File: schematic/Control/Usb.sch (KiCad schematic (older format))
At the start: 35 parts

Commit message: Control board diagram complete at high level - Clock, USB, Control, Power and IO done. Remaining is FPGA pin assignment which will be done later to optimize board layout.
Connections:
- net +3V3_USB renamed +3V3

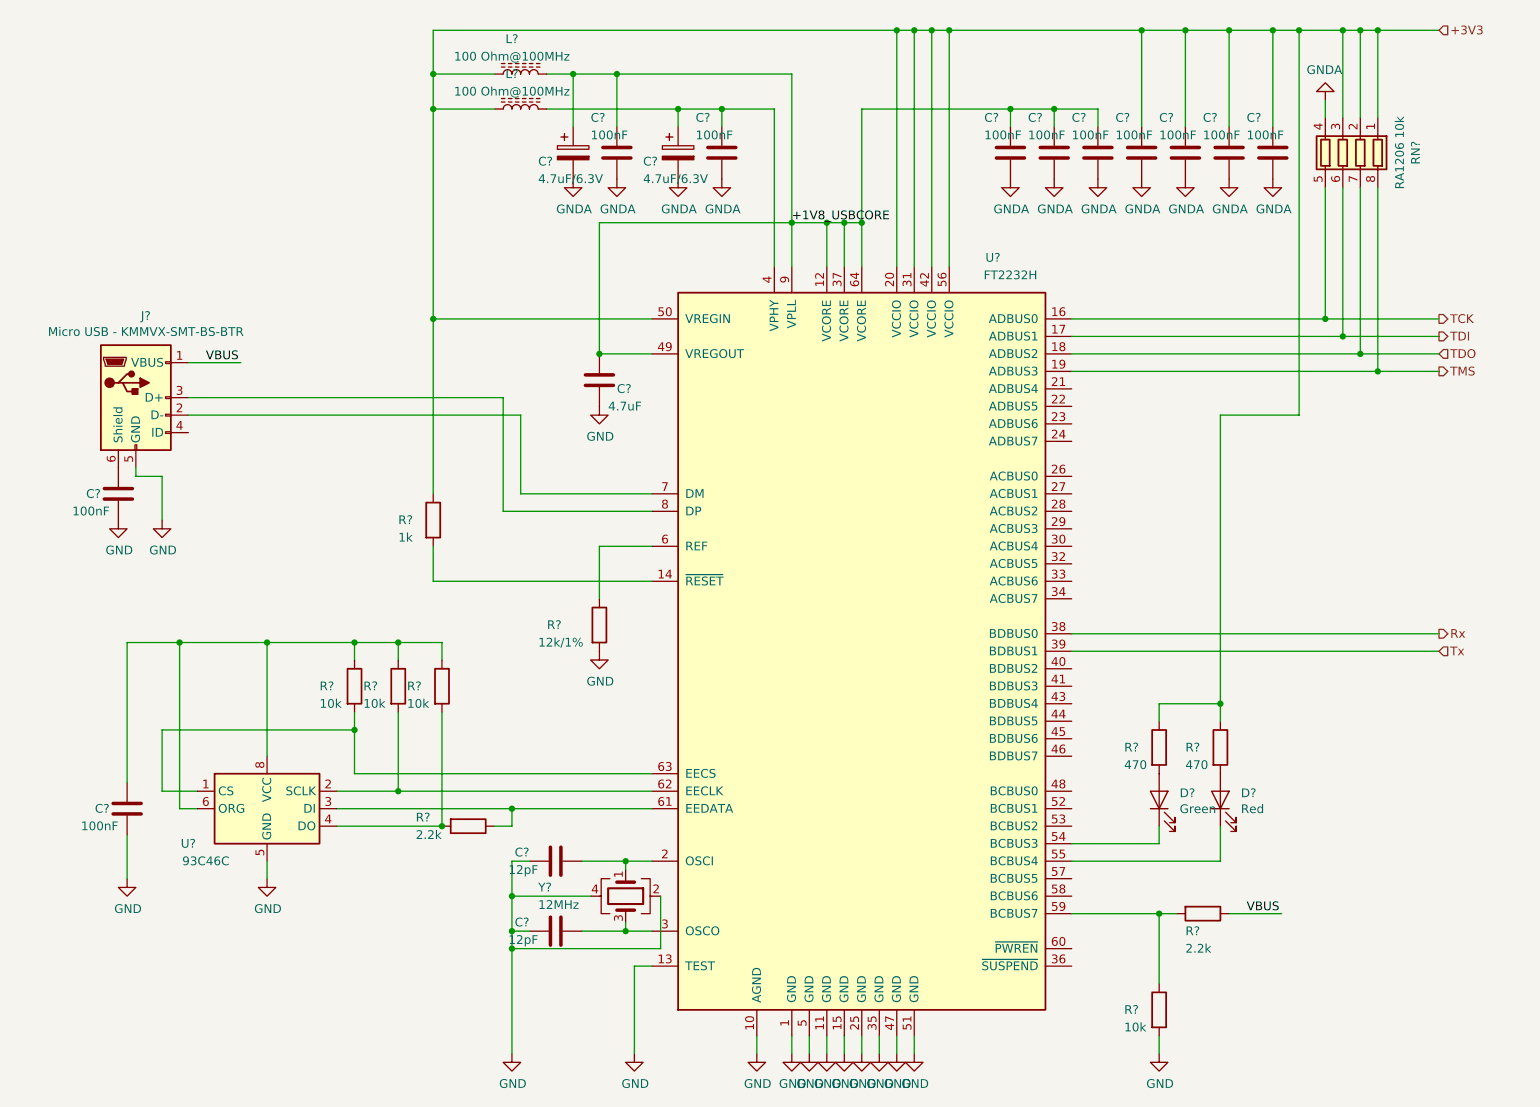
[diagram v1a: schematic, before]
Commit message: Provision for SPI Slave FPGA bitstream download. Switch RAM from x16 to x8 one.
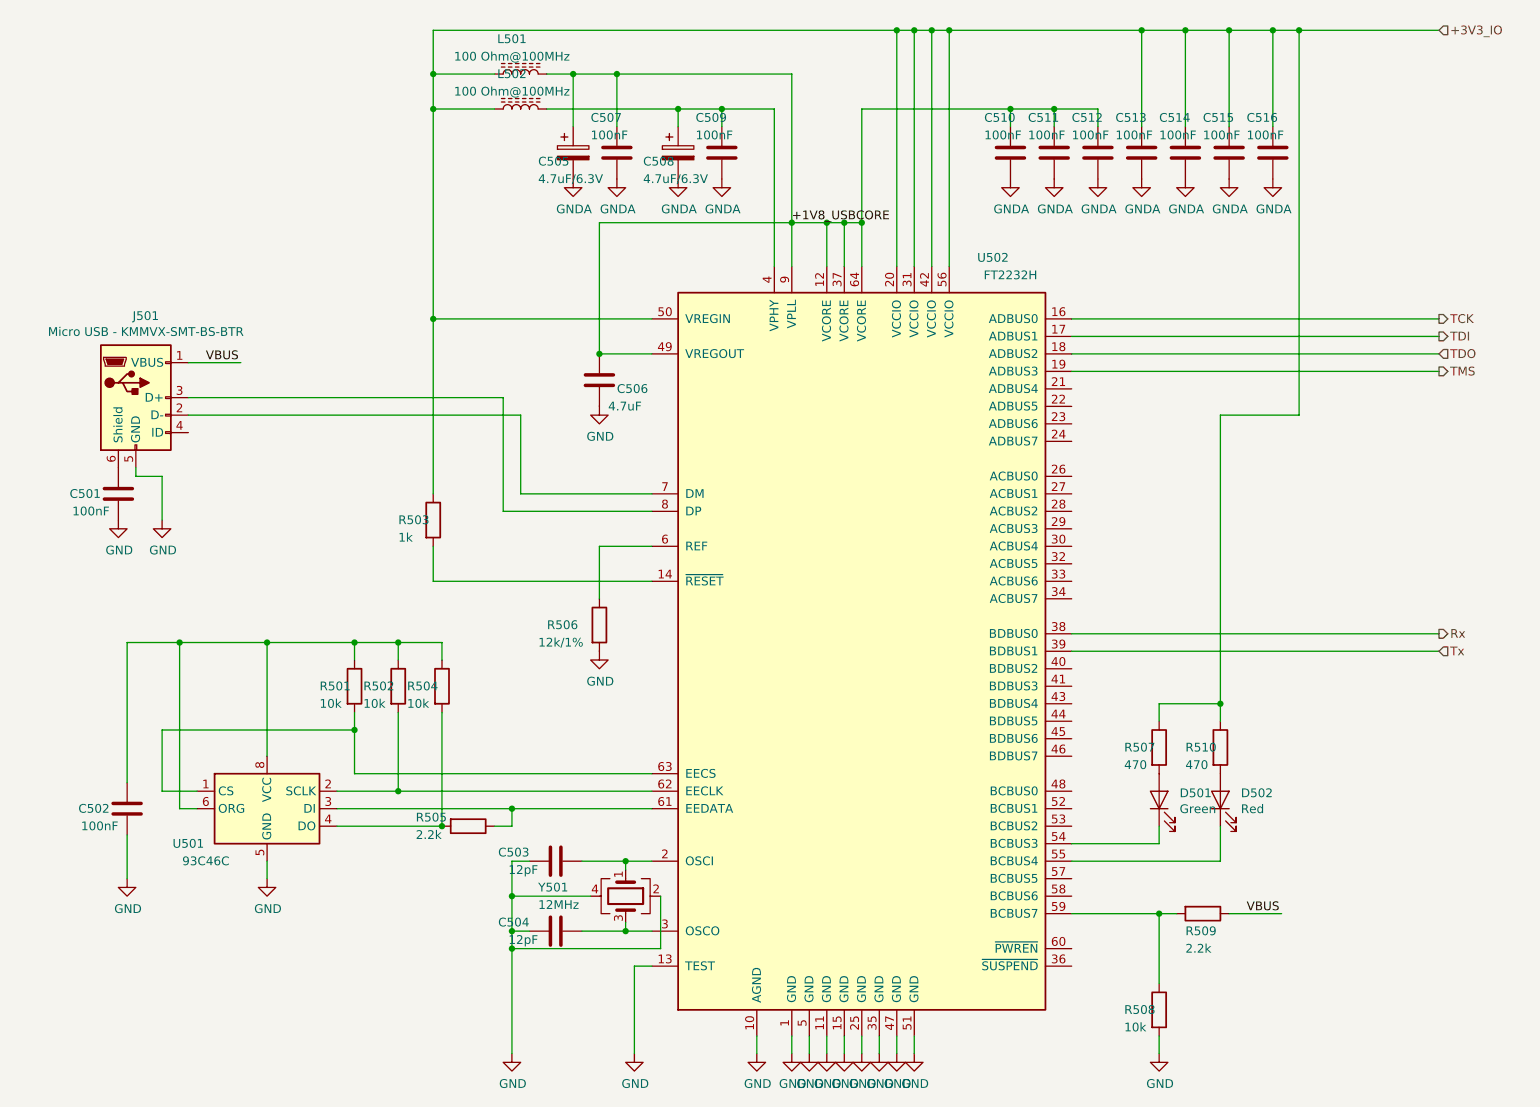
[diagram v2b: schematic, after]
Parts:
- removed RN?: RA1206 10k, Resistor_SMD:R_Array_Convex_4x0603, symbol Device:R_Pack04
- U501: renamed from U?; footprint (none) -> Package_SO:SOIC-8_3.9x4.9mm_P1.27mm
- Y501: renamed from Y?; footprint (none) -> Crystal:Crystal_SMD_3225-4Pin_3.2x2.5mm
- gave numbers to parts that had none: 32
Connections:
- net +3V3 renamed +3V3_IO

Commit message: Interim commit
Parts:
- removed D501: Green, LED_SMD:LED_0805_2012Metric, symbol Device:LED
- removed D502: Red, LED_SMD:LED_0805_2012Metric, symbol Device:LED
- removed R507, R510: 470, Resistor_SMD:R_0603_1608Metric, symbol Device:R
- added C517: 100nF, Capacitor_SMD:C_0603_1608Metric, symbol Device:C
- J501: footprint Zmei_Footprints:USB_MICRO_KMMVX-SMT-BS-BTR -> Zmei_Footprints:USB_MICRO_207A-BBA0-R
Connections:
- net GNDA is gone; now on net GND: C505.2, C507.2, C508.2, C509.2, C510.2, C511.2, C512.2, C513.2, C514.2, C515.2, C516.2
- net +1V8_USBCORE: no longer C505.1, C507.1, L501.2, U502.9 (VPLL)
- net +3V3_IO: now also C502.2, R501.1, R502.1, R504.1, U501.6 (ORG), U501.8 (VCC), C517.1
- net GND: now also C517.2
- net RXLED: now reaches U502.54 (BCBUS3)
- net TXLED: now reaches U502.55 (BCBUS4)
- new net: C505.1, C507.1, L501.2, U502.9 (VPLL)
